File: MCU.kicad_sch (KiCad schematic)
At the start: 21 parts, among them U7 STM32F405RGTx, U8 8Mhz,50ppm

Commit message: update
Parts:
- removed BOOT1: Jumper_2_Open, Connector_PinHeader_2.54mm:PinHeader_1x02_P2.54mm_Vertical, symbol Jumper:Jumper_2_Open
- added SW1: SSSS213000, mylib:SSSS213000, symbol SSSS213000:SSSS213000
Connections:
- net +3.3V: now also SW1.1 (NO)
- net BOOT0: now also SW1.2 (C)
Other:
- moved on the sheet: R9
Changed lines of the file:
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@@
 	)
 	(junction
-		(at 154.94 148.59)
-		(diameter 0)
-		(color 0 0 0 0)
-	)
-	(junction
 		(at 69.85 53.34)
 		(diameter 0)
@@
 	)
 	(junction
+		(at 171.45 144.78)
+		(diameter 0)
+		(color 0 0 0 0)
+	)
+	(junction
 		(at 148.59 45.72)
 		(diameter 0)
@@
 	(wire
 		(pts
+			(xy 148.59 142.24) (xy 149.86 142.24)
+		)
+		(stroke
+			(width 0)
+			(type default)
+		)
+	)
+	(wire
+		(pts
 			(xy 250.19 134.62) (xy 250.19 138.43)
 		)
@@
 	(wire
 		(pts
-			(xy 154.94 147.32) (xy 154.94 148.59)
+			(xy 171.45 143.51) (xy 171.45 144.78)
 		)
 		(stroke
@@
 	(wire
 		(pts
-			(xy 149.86 148.59) (xy 154.94 148.59)
-		)
-		(stroke
-			(width 0)
-			(type default)
-		)
-	)
-	(wire
-		(pts
 			(xy 90.17 81.28) (xy 90.17 83.82)
 		)
@@
 	(global_label "BOOT0"
 		(shape input)
-		(at 154.94 147.32 90)
+		(at 171.45 143.51 90)
 		(effects
 			(font
@@
 		)
 		(property "Intersheetrefs" "${INTERSHEET_REFS}"
-			(at 154.94 147.32 90)
+			(at 171.45 143.51 90)
 			(effects
 				(font
@@
 		(on_board yes)
 		(dnp no)
-		(property "Reference" "#PWR051"
+		(property "Reference" "#PWR050"
 			(at 148.59 49.53 0)
 			(effects
@@
 			(project "MX_IMU"
 				(path "/8ed38441-7d4e-4e89-870f-07e11c6dce38/39c93069-edc2-4035-8fc7-27a45736847d"
-					(reference "#PWR051")
+					(reference "#PWR050")
 					(unit 1)
 				)
@@
 	)
 	(symbol
+		(lib_id "SSSS213000:SSSS213000")
+		(at 171.45 144.78 180)
+		(unit 1)
+		(exclude_from_sim no)
+		(in_bom yes)
+		(on_board yes)
+		(dnp no)
+		(property "Reference" "SW1"
+			(at 160.02 136.906 0)
+			(effects
+				(font
+					(size 1.27 1.27)
+				)
+				(justify left)
+			)
+		)
+		(property "Value" "SSSS213000"
+			(at 160.0201 157.48 90)
+			(effects
+				(font
+					(size 1.27 1.27)
+				)
+				(justify left)
+				(hide yes)
+			)
+		)
+		(property "Footprint" "mylib:SSSS213000"
+			(at 152.4 49.86 0)
+			(effects
+				(font
+					(size 1.27 1.27)
+				)
+				(justify left top)
+				(hide yes)
+			)
+		)
+		(property "Datasheet" "https://www.alps.com/prod/info/E/HTML/Switch/Slide/SSSS2/SSSS213000.html"
+			(at 152.4 -50.14 0)
+			(effects
+				(font
+					(size 1.27 1.27)
+				)
+				(justify left top)
+				(hide yes)
+			)
+		)
+		(property "Description" "Slide Switches 1-pole 2-positions"
+			(at 171.45 144.78 0)
+			(effects
+				(font
+					(size 1.27 1.27)
+				)
+				(hide yes)
+			)
+		)
+		(property "Height" "5"
+			(at 152.4 -250.14 0)
+			(effects
+				(font
+					(size 1.27 1.27)
+				)
+				(justify left top)
+				(hide yes)
+			)
+		)
+		(property "Avnet Part Number" ""
+			(at 152.4 -350.14 0)
+			(effects
+				(font
+					(size 1.27 1.27)
+				)
+				(justify left top)
+				(hide yes)
+			)
+		)
+		(property "Avnet Price/Stock" ""
+			(at 152.4 -450.14 0)
+			(effects
+				(font
+					(size 1.27 1.27)
+				)
+				(justify left top)
+				(hide yes)
+			)
+		)
+		(property "Manufacturer_Name" "ALPS Electric"
+			(at 152.4 -550.14 0)
+			(effects
+				(font
+					(size 1.27 1.27)
+				)
+				(justify left top)
+				(hide yes)
+			)
+		)
+		(property "Manufacturer_Part_Number" "SSSS213000"
+			(at 152.4 -650.14 0)
+			(effects
+				(font
+					(size 1.27 1.27)
+				)
+				(justify left top)
+				(hide yes)
+			)
+		)
+		(pin "3"
+		)
+		(pin "1"
+		)
+		(pin "2"
+		)
+		(instances
+			(project "MX_IMU"
+				(path "/8ed38441-7d4e-4e89-870f-07e11c6dce38/39c93069-edc2-4035-8fc7-27a45736847d"
+					(reference "SW1")
+					(unit 1)
+				)
+			)
+		)
+	)
+	(symbol
 		(lib_id "Device:C_Small")
 		(at 243.84 143.51 180)
@@
 		(on_board yes)
 		(dnp no)
-		(property "Reference" "#PWR054"
+		(property "Reference" "#PWR053"
 			(at 168.91 85.09 0)
 			(effects
@@
 			(project "MX_IMU"
 				(path "/8ed38441-7d4e-4e89-870f-07e11c6dce38/39c93069-edc2-4035-8fc7-27a45736847d"
-					(reference "#PWR054")
+					(reference "#PWR053")
 					(unit 1)
 				)
@@
 	)
 	(symbol
-		(lib_id "Jumper:Jumper_2_Open")
-		(at 144.78 148.59 0)
-		(unit 1)
-		(exclude_from_sim no)
-		(in_bom yes)
-		(on_board yes)
-		(dnp no)
-		(property "Reference" "BOOT1"
-			(at 144.78 143.2392 0)
-			(effects
-				(font
-					(size 1.27 1.27)
-				)
-			)
-		)
-		(property "Value" "Jumper_2_Open"
-			(at 144.78 145.7761 0)
-			(effects
-				(font
-					(size 1.27 1.27)
-				)
-			)
-		)
-		(property "Footprint" "Connector_PinHeader_2.54mm:PinHeader_1x02_P2.54mm_Vertical"
-			(at 144.78 148.59 0)
-			(effects
-				(font
-					(size 1.27 1.27)
-				)
-				(hide yes)
-			)
-		)
-		(property "Datasheet" "~"
-			(at 144.78 148.59 0)
-			(effects
-				(font
-					(size 1.27 1.27)
-				)
-				(hide yes)
-			)
-		)
-		(property "Description" ""
-			(at 144.78 148.59 0)
-			(effects
-				(font
-					(size 1.27 1.27)
-				)
-			)
-		)
-		(pin "1"
-		)
-		(pin "2"
-		)
-		(instances
-			(project "MX_IMU"
-				(path "/8ed38441-7d4e-4e89-870f-07e11c6dce38/39c93069-edc2-4035-8fc7-27a45736847d"
-					(reference "BOOT1")
-					(unit 1)
-				)
-			)
-		)
-	)
-	(symbol
 		(lib_id "power:PWR_FLAG")
 		(at 140.97 45.72 0)
@@
 	(symbol
 		(lib_id "power:+3.3V")
-		(at 139.7 148.59 90)
+		(at 149.86 142.24 90)
 		(unit 1)
 		(exclude_from_sim no)
@@
 		(on_board yes)
 		(dnp no)
-		(property "Reference" "#PWR050"
-			(at 143.51 148.59 0)
+		(property "Reference" "#PWR051"
+			(at 153.67 142.24 0)
 			(effects
 				(font
@@
 		)
 		(property "Value" "+3.3V"
-			(at 138.176 151.13 90)
+			(at 148.336 144.78 90)
 			(effects
 				(font
@@
 		)
 		(property "Footprint" ""
-			(at 139.7 148.59 0)
+			(at 149.86 142.24 0)
 			(effects
 				(font
@@
 		)
 		(property "Datasheet" ""
-			(at 139.7 148.59 0)
+			(at 149.86 142.24 0)
 			(effects
 				(font
@@
 		)
 		(property "Description" "Power symbol creates a global label with name \"+3.3V\""
-			(at 139.7 148.59 0)
+			(at 149.86 142.24 0)
 			(effects
 				(font
@@
 			(project "MX_IMU"
 				(path "/8ed38441-7d4e-4e89-870f-07e11c6dce38/39c93069-edc2-4035-8fc7-27a45736847d"
-					(reference "#PWR050")
+					(reference "#PWR051")
 					(unit 1)
 				)
@@
 		(dnp no)
 		(fields_autoplaced yes)
-		(property "Reference" "#PWR055"
+		(property "Reference" "#PWR054"
 			(at 165.1 111.76 0)
 			(effects
@@
 			(project "MX_IMU"
 				(path "/8ed38441-7d4e-4e89-870f-07e11c6dce38/39c93069-edc2-4035-8fc7-27a45736847d"
-					(reference "#PWR055")
+					(reference "#PWR054")
 					(unit 1)
 				)
@@
 	(symbol
 		(lib_id "power:GND")
-		(at 154.94 156.21 0)
+		(at 171.45 152.4 0)
 		(unit 1)
 		(exclude_from_sim no)
@@
 		(dnp no)
 		(fields_autoplaced yes)
-		(property "Reference" "#PWR053"
-			(at 154.94 162.56 0)
+		(property "Reference" "#PWR055"
+			(at 171.45 158.75 0)
 			(effects
 				(font
@@
 		)
 		(property "Value" "GND"
-			(at 154.94 161.29 0)
+			(at 171.45 157.48 0)
 			(effects
 				(font
@@
 		)
 		(property "Footprint" ""
-			(at 154.94 156.21 0)
+			(at 171.45 152.4 0)
 			(effects
 				(font
@@
 		)
 		(property "Datasheet" ""
-			(at 154.94 156.21 0)
+			(at 171.45 152.4 0)
 			(effects
 				(font
@@
 		)
 		(property "Description" "Power symbol creates a global label with name \"GND\" , ground"
-			(at 154.94 156.21 0)
+			(at 171.45 152.4 0)
 			(effects
 				(font
@@
 			(project "MX_IMU"
 				(path "/8ed38441-7d4e-4e89-870f-07e11c6dce38/39c93069-edc2-4035-8fc7-27a45736847d"
-					(reference "#PWR053")
+					(reference "#PWR055")
 					(unit 1)
 				)
@@
 	(symbol
 		(lib_id "Device:R")
-		(at 154.94 152.4 0)
+		(at 171.45 148.59 0)
 		(unit 1)
 		(exclude_from_sim no)
@@
 		(dnp no)
 		(property "Reference" "R9"
-			(at 150.876 151.13 0)
+			(at 167.386 147.32 0)
 			(effects
 				(font
@@
 		)
 		(property "Value" "10k"
-			(at 149.86 153.67 0)
+			(at 166.37 149.86 0)
 			(effects
 				(font
@@
 		)
 		(property "Footprint" "Resistor_SMD:R_0603_1608Metric"
-			(at 153.162 152.4 90)
+			(at 169.672 148.59 90)
 			(effects
 				(font
@@
 		)
 		(property "Datasheet" "~"
-			(at 154.94 152.4 0)
+			(at 171.45 148.59 0)
 			(effects
 				(font
@@
 		)
 		(property "Description" "Resistor"
-			(at 154.94 152.4 0)
+			(at 171.45 148.59 0)
 			(effects
 				(font

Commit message: update
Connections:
- net GYRO_LSE: now reaches U7.30 (PB11)
- net GYRO_INT2: no longer names the net of U7.41 (PA8)
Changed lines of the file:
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@@
+	)
+	(no_connect
+		(at 102.87 111.76)
 	)
 	(no_connect
 		(at 62.23 116.84)
-	)
-	(no_connect
-		(at 102.87 162.56)
 	)
 	(no_connect
@@
 		)
 	)
+	(global_label "GYRO_LSE"
+		(shape input)
+		(at 102.87 162.56 0)
+		(effects
+			(font
+				(size 1.27 1.27)
+			)
+			(justify left)
+		)
+		(property "Intersheetrefs" "${INTERSHEET_REFS}"
+			(at 102.87 162.56 0)
+			(effects
+				(font
+					(size 1.27 1.27)
+				)
+				(hide yes)
+			)
+		)
+	)
 	(global_label "GPS_RX"
 		(shape input)
@@
 		(property "Intersheetrefs" "${INTERSHEET_REFS}"
 			(at 62.23 142.24 0)
+			(effects
+				(font
+					(size 1.27 1.27)
+				)
+				(hide yes)
+			)
+		)
+	)
+	(global_label "GYRO_LSE"
+		(shape input)
+		(at 143.51 173.99 0)
+		(effects
+			(font
+				(size 1.27 1.27)
+			)
+			(justify left)
+		)
+		(property "Intersheetrefs" "${INTERSHEET_REFS}"
+			(at 143.51 173.99 0)
 			(effects
 				(font
@@
 				(hide yes)
 			)
-		)
-	)
-	(global_label "GYRO_INT2"
-		(shape input)
-		(at 102.87 111.76 0)
-		(effects
-			(font
-				(size 1.27 1.27)
-			)
-			(justify left)
-		)
-		(property "Intersheetrefs" "${INTERSHEET_REFS}"
-			(at 102.87 111.76 0)
-			(effects
-				(font
-					(size 1.27 1.27)
-				)
-				(hide yes)
-			)

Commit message: update
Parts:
- renumbered SW1 to SW2
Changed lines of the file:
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@@
 		(on_board yes)
 		(dnp no)
-		(property "Reference" "SW1"
+		(property "Reference" "SW2"
 			(at 160.02 136.906 0)
 			(effects
@@
 			(project "MX_IMU"
 				(path "/8ed38441-7d4e-4e89-870f-07e11c6dce38/39c93069-edc2-4035-8fc7-27a45736847d"
-					(reference "SW1")
+					(reference "SW2")
 					(unit 1)
 				)

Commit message: update
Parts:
- renumbered C12 to C11, C14 to C12, C15 to C13, C16 to C14, C17 to C15, C18 to C16, C19 to C17, C20 to C18, C22 to C19, C21 to C20, C11 to C21, C13 to C22, U8 to U7, U7 to U8
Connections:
- net BARO_INT: now reaches U8.59 (PB7)
- net GPS_SCL renamed Baro_SCL
- net GPS_SDA renamed Baro_SDA
- no-connect marks 23 -> 22

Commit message: update
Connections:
- net Status_LED: now also U8.37 (PC6)
- net Tim8_2: now reaches U8.38 (PC7)
- net Tim8_3: now reaches U8.39 (PC8)
- net Tim8_4: now reaches U8.40 (PC9)
- no-connect marks 22 -> 19
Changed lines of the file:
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@@
 	)
 	(no_connect
+		(at 148.59 144.78)
+	)
+	(no_connect
 		(at 62.23 152.4)
 	)
@@
 	)
 	(no_connect
-		(at 62.23 134.62)
-	)
-	(no_connect
-		(at 62.23 129.54)
-	)
-	(no_connect
 		(at 62.23 147.32)
 	)
@@
 	)
 	(no_connect
-		(at 62.23 137.16)
-	)
-	(no_connect
 		(at 62.23 109.22)
 	)
@@
 	)
 	(no_connect
-		(at 62.23 132.08)
-	)
-	(no_connect
 		(at 62.23 121.92)
 	)
@@
 		)
 	)
+	(global_label "Tim8_4"
+		(shape input)
+		(at 62.23 137.16 180)
+		(effects
+			(font
+				(size 1.27 1.27)
+			)
+			(justify right)
+		)
+		(property "Intersheetrefs" "${INTERSHEET_REFS}"
+			(at 62.23 137.16 0)
+			(effects
+				(font
+					(size 1.27 1.27)
+				)
+				(hide yes)
+			)
+		)
+	)
 	(global_label "Native_D-"
 		(shape input)
@@
 	(global_label "Status_LED"
 		(shape input)
-		(at 109.22 80.01 0)
+		(at 62.23 129.54 180)
 		(fields_autoplaced yes)
 		(effects
@@
 				(size 1.27 1.27)
 			)
-			(justify left)
+			(justify right)
 		)
 		(property "Intersheetrefs" "${INTERSHEET_REFS}"
-			(at 122.6069 80.01 0)
+			(at 48.8431 129.54 0)
 			(effects
 				(font
 					(size 1.27 1.27)
 				)
-				(justify left)
+				(justify right)
 				(hide yes)
 			)
@@
 		)
 	)
+	(global_label "Tim8_3"
+		(shape input)
+		(at 62.23 134.62 180)
+		(effects
+			(font
+				(size 1.27 1.27)
+			)
+			(justify right)
+		)
+		(property "Intersheetrefs" "${INTERSHEET_REFS}"
+			(at 62.23 134.62 0)
+			(effects
+				(font
+					(size 1.27 1.27)
+				)
+				(hide yes)
+			)
+		)
+	)
 	(global_label "SWO"
 		(shape input)
@@
 		)
 	)
+	(global_label "Tim8_2"
+		(shape input)
+		(at 62.23 132.08 180)
+		(effects
+			(font
+				(size 1.27 1.27)
+			)
+			(justify right)
+		)
+		(property "Intersheetrefs" "${INTERSHEET_REFS}"
+			(at 62.23 132.08 0)
+			(effects
+				(font
+					(size 1.27 1.27)
+				)
+				(hide yes)
+			)
+		)
+	)
 	(global_label "HSE_IN"
 		(shape input)
@@
 		)
 		(property "Value" "+3.3V"
-			(at 148.336 144.78 90)
+			(at 146.558 138.43 90)
 			(effects
 				(font

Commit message: update
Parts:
- renumbered C21 to C11, C11 to C12, C22 to C13, C12 to C14, C13 to C15, C14 to C16, C15 to C17, C16 to C18, C17 to C19, C18 to C20, C20 to C21, C19 to C22, U8 to U7, U7 to U8

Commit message: PumbaaV2_RC2
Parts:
- removed R9: 10k, Resistor_SMD:R_0603_1608Metric, symbol Device:R
- added R9: 10k, Resistor_SMD:R_0402_1005Metric, symbol Device:R_Small
- MainLED1: footprint LED_SMD:LED_WS2812B-2020_PLCC4_2.0x2.0mm -> LED_SMD:LED_WS2812B_PLCC4_5.0x5.0mm_P3.2mm; LCSC Part (none) -> C965555
- Reset1: footprint Button_Switch_THT:SW_PUSH_6mm -> Button_Switch_THT:SW_PUSH_6mm_H5mm; LCSC Part (none) -> C455109
- SW2: LCSC Part  (none) -> C125054
- U8: value 8Mhz,50ppm -> X1G0059610004; footprint Oscillator:Oscillator_SMD_SeikoEpson_SG8002CE-4Pin_3.2x2.5mm -> mylib:Oscillator_SMD_SeikoEpson_SG3225CAN-4Pin_3.2x2.5mm; CPN BT05001-12601 -> (none); LCSC Part  (none) -> C7504299; MPN SG3225CAN 12.0000M-TJGA6 -> X1G0059610004
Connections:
- net BOOT0: now also R9.1
- net GND: now also R9.2
- net BARO_INT renamed Baro_INT

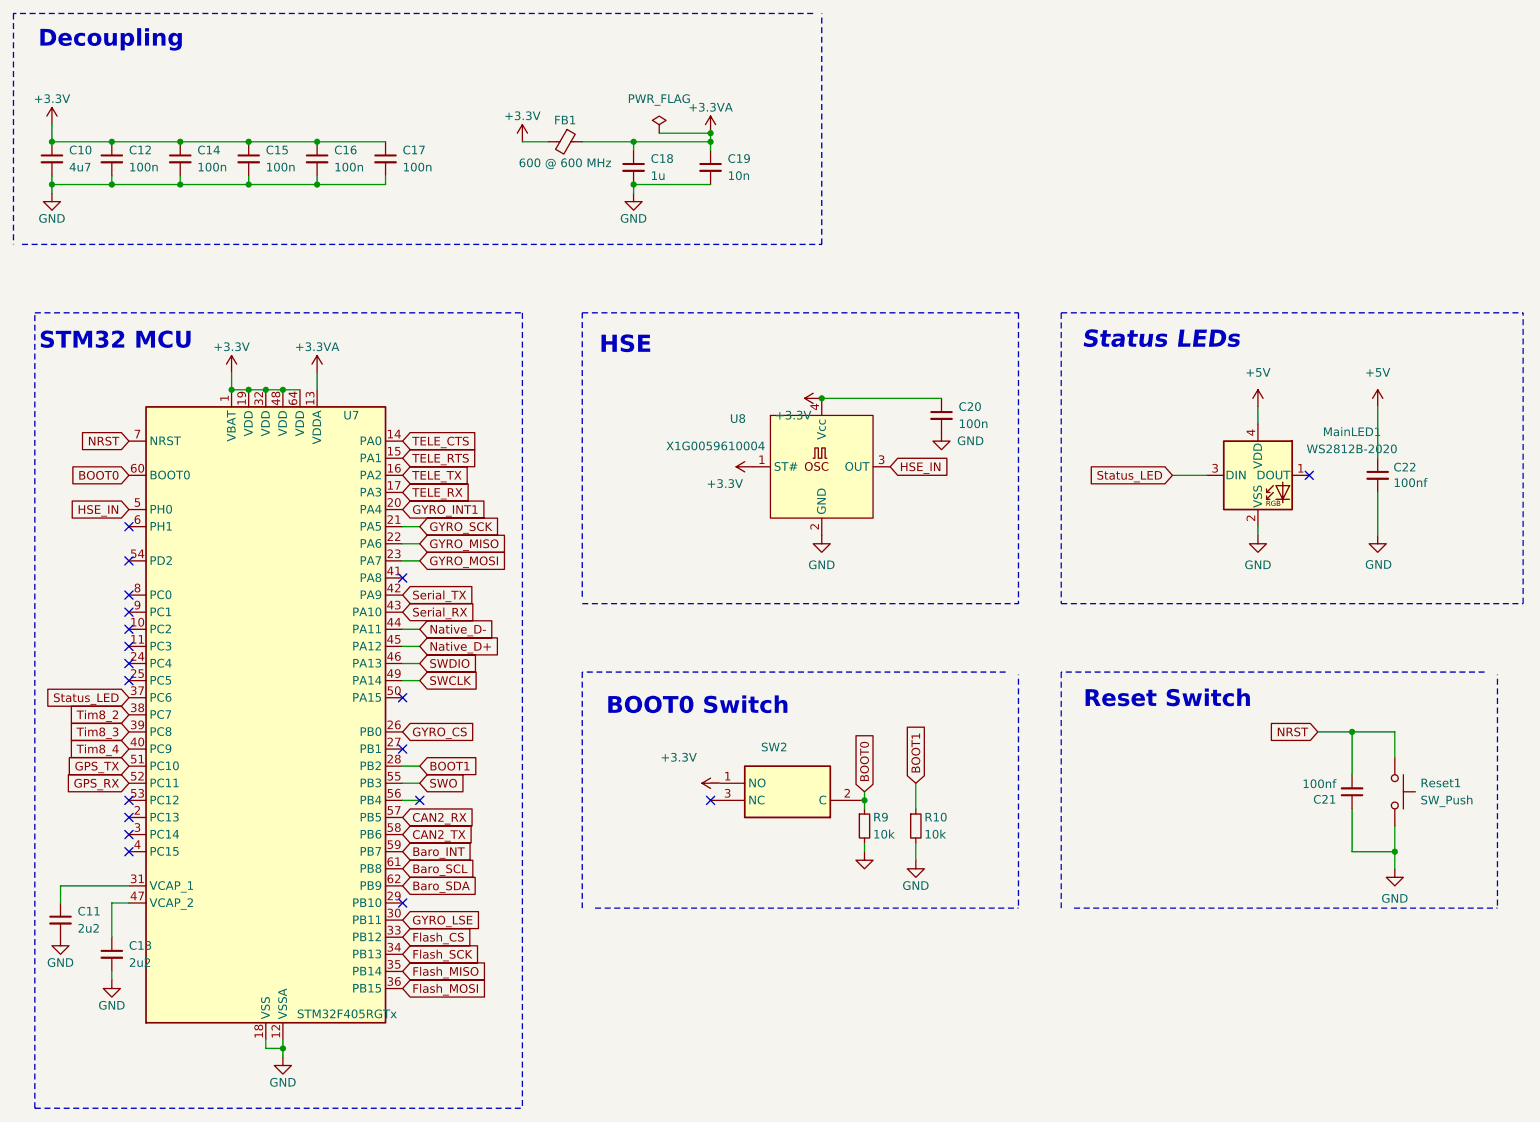
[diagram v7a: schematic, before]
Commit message: compact  IMU module for integration
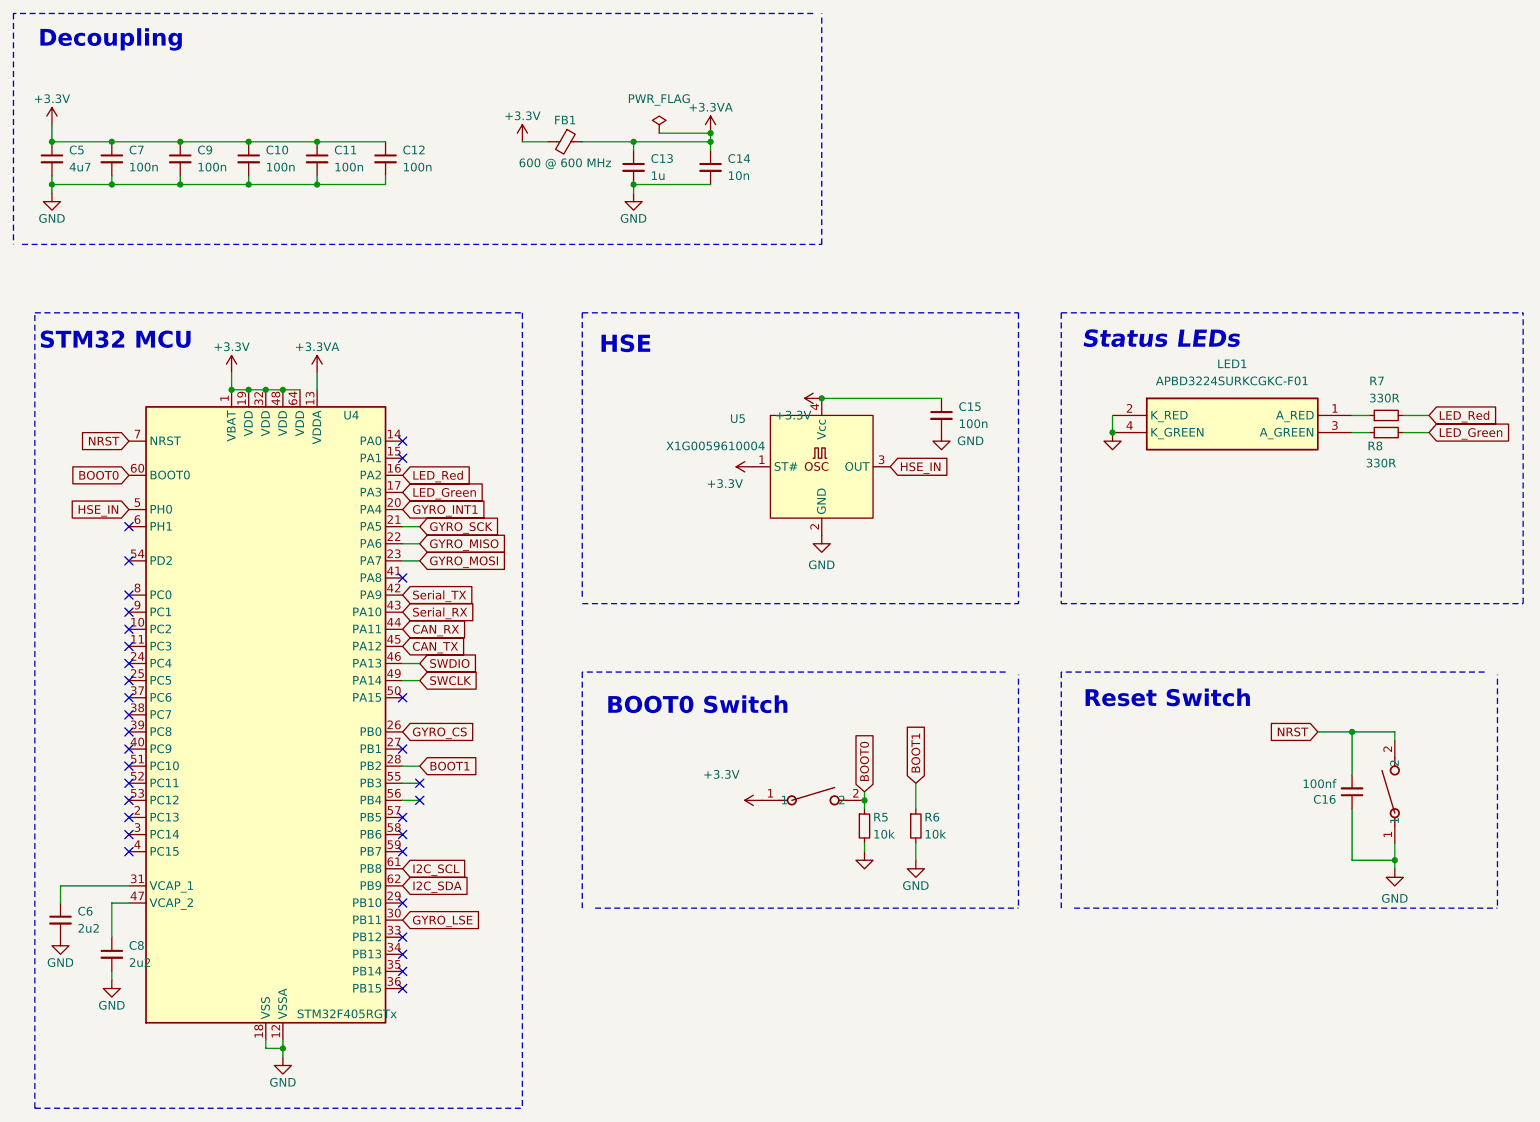
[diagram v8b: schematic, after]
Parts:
- removed C22: 100nf, Capacitor_SMD:C_0603_1608Metric, symbol Device:C_Small
- removed MainLED1: WS2812B-2020, LED_SMD:LED_WS2812B_PLCC4_5.0x5.0mm_P3.2mm, symbol LED:WS2812B-2020
- removed Reset1: SW_Push, Button_Switch_THT:SW_PUSH_6mm_H5mm, symbol Switch:SW_Push
- removed SW2: SSSS213000, mylib:SSSS213000, symbol SSSS213000:SSSS213000
- added LED1: APBD3224SURKCGKC-F01, mylib:APBD3224SURKCGKCF01, symbol APBD3224SURKCGKC-F01:APBD3224SURKCGKC-F01
- added R7, R8: 330R, Resistor_SMD:R_0402_1005Metric, symbol Device:R_Small
- added SW1, SW2: B3U-1000P, mylib:SW_B3U-1000P_OMR, symbol SW_B3U-1000P:B3U-1000P[]
- renumbered C15 to C10, C16 to C11, C17 to C12, C18 to C13, C19 to C14, C20 to C15, C21 to C16, C10 to C5, C11 to C6, C12 to C7, C13 to C8, C14 to C9, R9 to R5, R10 to R6, U7 to U4, U8 to U5
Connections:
- net +3.3V: now also SW1.1
- net BOOT0: now also SW1.2
- net GND: now also LED1.2 (K_RED), LED1.4 (K_GREEN), SW2.1
- net NRST: now also SW2.2
- net Baro_INT: no longer names the net of U4.59 (PB7)
- net Baro_SCL renamed I2C_SCL
- net Baro_SDA renamed I2C_SDA
- net CAN2_RX: no longer names the net of U4.57 (PB5)
- net CAN2_TX: no longer names the net of U4.58 (PB6)
- net Flash_CS: no longer names the net of U4.33 (PB12)
- net Flash_MISO: no longer names the net of U4.35 (PB14)
- net Flash_MOSI: no longer names the net of U4.36 (PB15)
- net Flash_SCK: no longer names the net of U4.34 (PB13)
- net GPS_RX: no longer names the net of U4.52 (PC11)
- net GPS_TX: no longer names the net of U4.51 (PC10)
- net Native_D+ renamed CAN_TX
- net Native_D- renamed CAN_RX
- net SWO: no longer names the net of U4.55 (PB3)
- net Status_LED: no longer names the net of U4.37 (PC6)
- net TELE_CTS: no longer names the net of U4.14 (PA0)
- net TELE_RTS: no longer names the net of U4.15 (PA1)
- net TELE_RX renamed LED_Green
- net LED_Green: now also R8.2
- net TELE_TX renamed LED_Red
- net LED_Red: now also R7.2
- net Tim8_2: no longer names the net of U4.38 (PC7)
- net Tim8_3: no longer names the net of U4.39 (PC8)
- net Tim8_4: no longer names the net of U4.40 (PC9)
- new net: LED1.1 (A_RED), R7.1
- new net: LED1.3 (A_GREEN), R8.1
- no-connect marks 19 -> 33
